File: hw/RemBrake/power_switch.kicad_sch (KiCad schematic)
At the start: 36 parts, among them Q5 BC337, Q6 SiS415DNT, Q7 BC847, Q8 BC337, Q9 BC847, U10 BD48ExxG, U3 TPS62140, U4 XC6220B331MR, U8 MAX40200AUK

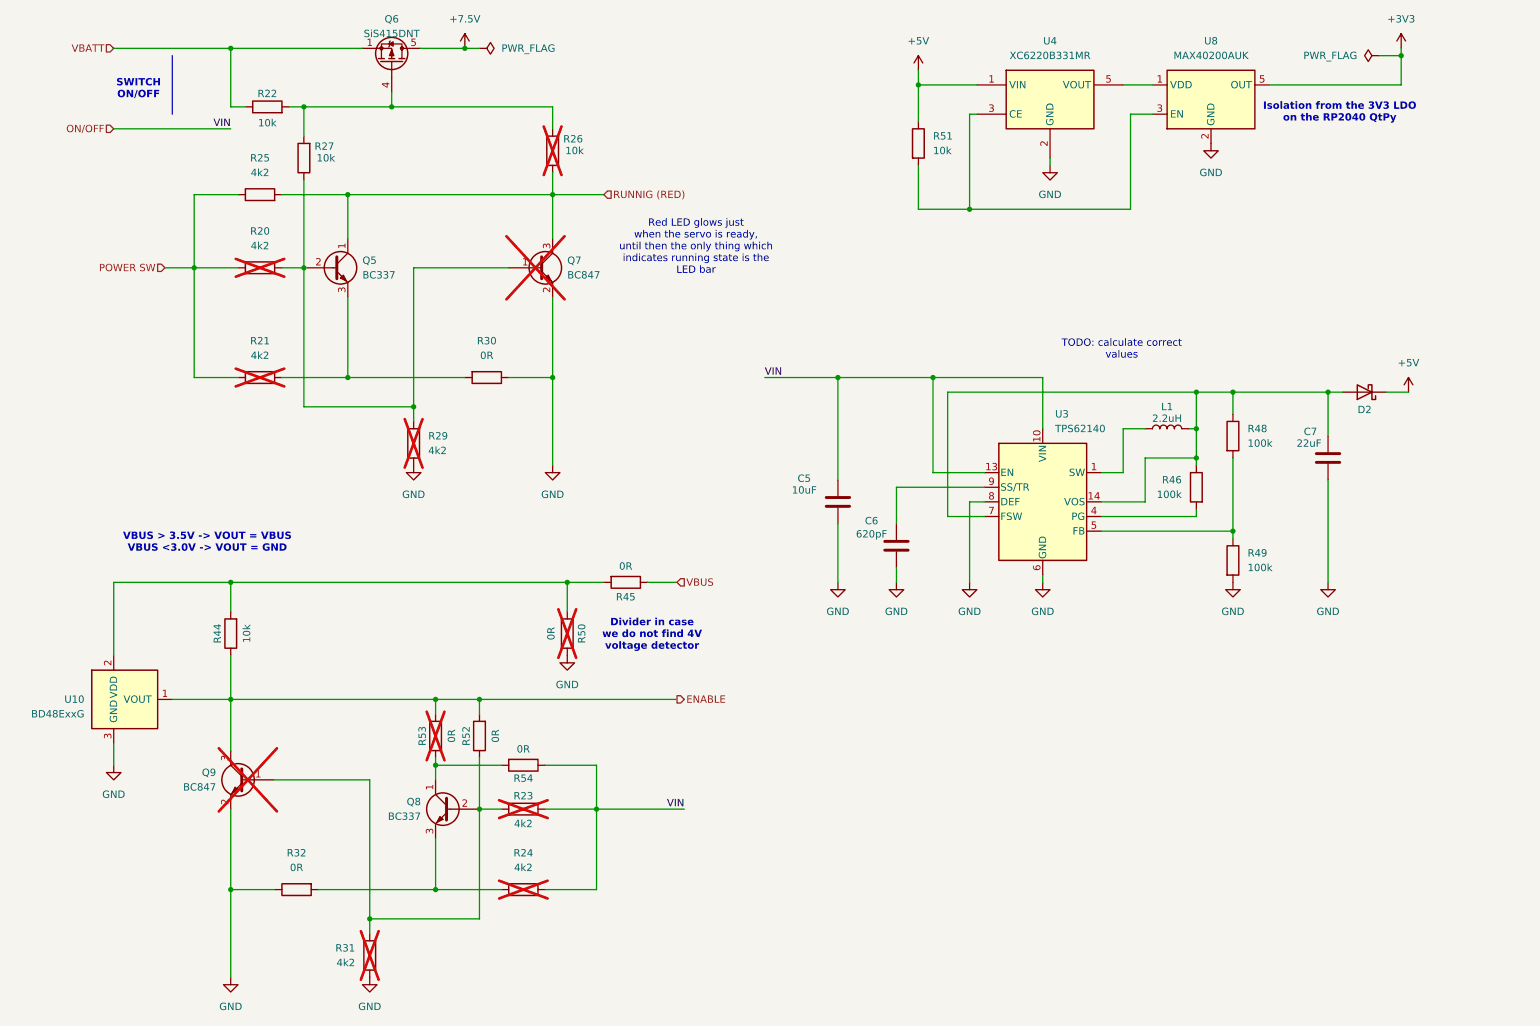
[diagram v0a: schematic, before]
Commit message: project renamed, schematics changed based on breakout boards notes and created new layout with better connectors
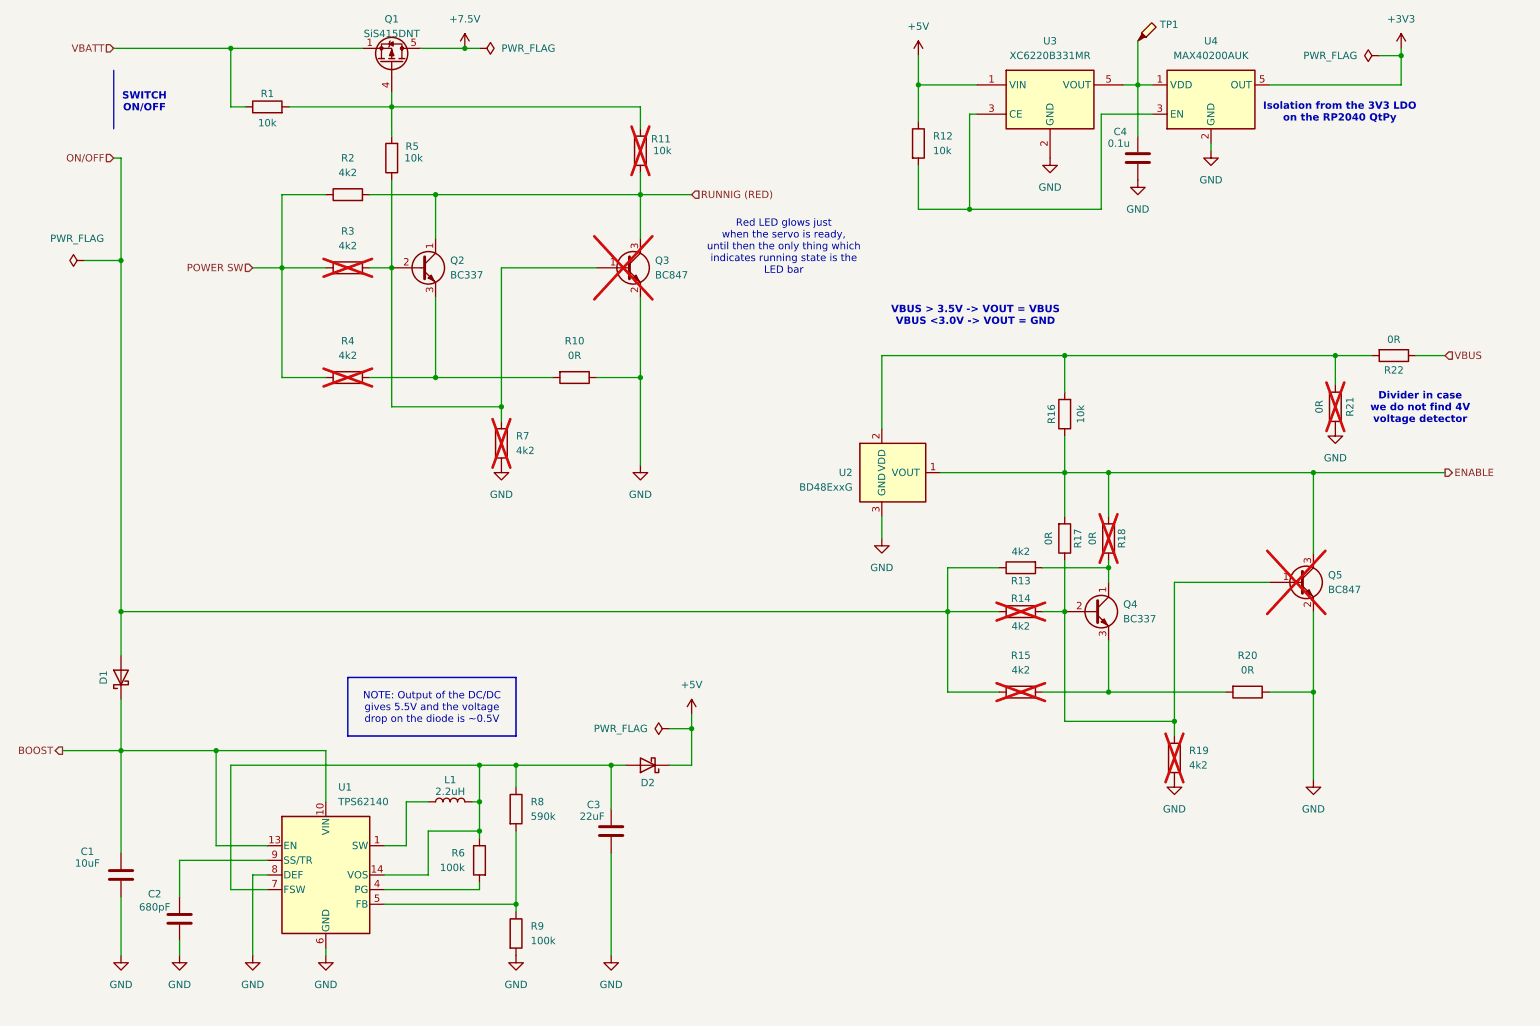
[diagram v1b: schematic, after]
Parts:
- added C4: 0.1u, Capacitor_SMD:C_0805_2012Metric_Pad1.18x1.45mm_HandSolder, symbol Device:C
- added D1: D_Schottky, Diode_SMD:D_SOD-128, symbol Device:D_Schottky
- added TP1: TestPoint_Probe, TestPoint:TestPoint_Pad_1.5x1.5mm, symbol Connector:TestPoint_Probe
- C2: renamed from C6; value 620pF -> 680pF
- D2: footprint (none) -> Diode_SMD:D_SOD-128; Purchase (none) -> https://cz.farnell.com/diodes-inc/mbr230s1f-7/schottky-rect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
- L1: footprint (none) -> Inductor_SMD:L_1008_2520Metric_Pad1.43x2.20mm_HandSolder; Purchase (none) -> https://cz.farnell.com/murata/dfe252012p-2r2m-p2/inductor-2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
- R13: renamed from R54; value 0R -> 4k2
- R8: renamed from R48; value 100k -> 590k
- renumbered C5 to C1, C7 to C3, Q6 to Q1, Q5 to Q2, Q7 to Q3, Q8 to Q4, Q9 to Q5, R22 to R1, R30 to R10, R26 to R11, R51 to R12, R23 to R14, R24 to R15, R44 to R16, R52 to R17, R53 to R18, R31 to R19, R25 to R2, R32 to R20, R50 to R21, R45 to R22, R20 to R3, R21 to R4, R27 to R5, R46 to R6, R29 to R7, R49 to R9, U3 to U1, U10 to U2, U4 to U3, U8 to U4
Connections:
- net GND: now also C4.2
- net ON/OFF: now also D1.2 (A); no longer C1.1, U1.10 (VIN), U1.11 (VIN), U1.12 (VIN), U1.13 (EN)
- net at U3.5 (VOUT), U4.1 (VDD): now also C4.1, TP1.1
- new net BOOST: C1.1, D1.1 (K), U1.10 (VIN), U1.11 (VIN), U1.12 (VIN), U1.13 (EN)
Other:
- note removed: "TODO: calculate correct values"
- moved on the sheet: C1, C2, C3, D2, L1, Q2, Q3, Q4, Q5, R10, R11, R13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

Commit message: added few components to fix indicator LED undefined cathode voltage and added vbus divider to match MCU voltage level
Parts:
- added R22: 10k, Resistor_SMD:R_0805_2012Metric_Pad1.20x1.40mm_HandSolder, symbol Device:R
- R7: value 4k2 -> 42k; now fitted
- renumbered R22 to R23
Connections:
- net ENABLE: now also R22.2
- net GND: now also R22.1
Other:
- note added: "Divide the VBUS to avoid busting the MCU"
- note added: "Divider for lower threshold voltage detectors"
- note added: "Red LED glows just when the servo is ready,until then the only thing whichindicates running state is the LED bar"
- note added: "TODO: add resistor to divide the vbus voltage"
- note removed: "Divider in case we do not find 4V voltage detector"
- note removed: "Red LED glows just when the servo is ready, until then the only thing which indicates running state is the LED bar"

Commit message: updated date and revision in the schematics
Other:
- company: (none) -> Pacner Bros Tech
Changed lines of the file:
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@@
 	(title_block
 		(title "Power Control")
-		(date "2024-12-15")
-		(rev "1.0")
+		(date "2025-02-23")
+		(rev "2.0")
+		(company "Pacner Bros Tech")
 	)
 	(text "VBUS > 3.5V -> VOUT = VBUS\nVBUS <3.0V -> VOUT = GND"

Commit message: updated annotation
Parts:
- added R11, R12: 0R, Resistor_SMD:R_0805_2012Metric_Pad1.20x1.40mm_HandSolder, symbol Device:R
- added R16, R2: 100k, Resistor_SMD:R_0805_2012Metric_Pad1.20x1.40mm_HandSolder, symbol Device:R
- C4: value 0.1u -> 0.1uF
- D1, D2: value D_Schottky -> MBR0520; footprint Diode_SMD:D_SOD-128 -> Diode_SMD:D_SOD-123
- Q3, Q5: now left out of the parts list
- R14: renamed from R11; now left out of the parts list
- R17: renamed from R13; value 4k2 -> 5k
- R18: renamed from R14; value 4k2 -> 5k; now left out of the parts list
- R19: renamed from R15; value 4k2 -> 5k; now left out of the parts list
- R22: renamed from R18; now left out of the parts list
- R23: renamed from R19; value 4k2 -> 5k; now left out of the parts list
- R25: renamed from R21; now left out of the parts list
- R3: renamed from R2; value 4k2 -> 5k
- R4: renamed from R3; value 4k2 -> 5k; now left out of the parts list
- R5: renamed from R4; value 4k2 -> 5k; now left out of the parts list
- R8: renamed from R7; value 42k -> 0R; now not fitted; now left out of the parts list
- renumbered R9 to R10, R10 to R13, R12 to R15, R16 to R20, R17 to R21, R20 to R24, R22 to R26, R23 to R27, R5 to R6, R6 to R7, R8 to R9
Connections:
- net GND: now also R16.1, R2.1
- net ON/OFF: now also R16.2
- net POWER SW: now also R2.2
- net RUNNIG (RED): now also R11.1, R12.1; no longer Q2.1 (C), R3.2
- net at Q2.2 (B), Q3.1 (B), R4.2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: now also R12.2
- new net: Q2.1 (C), R11.2, R3.2
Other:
- note removed: "TODO: add resistor to divide the vbus voltage"

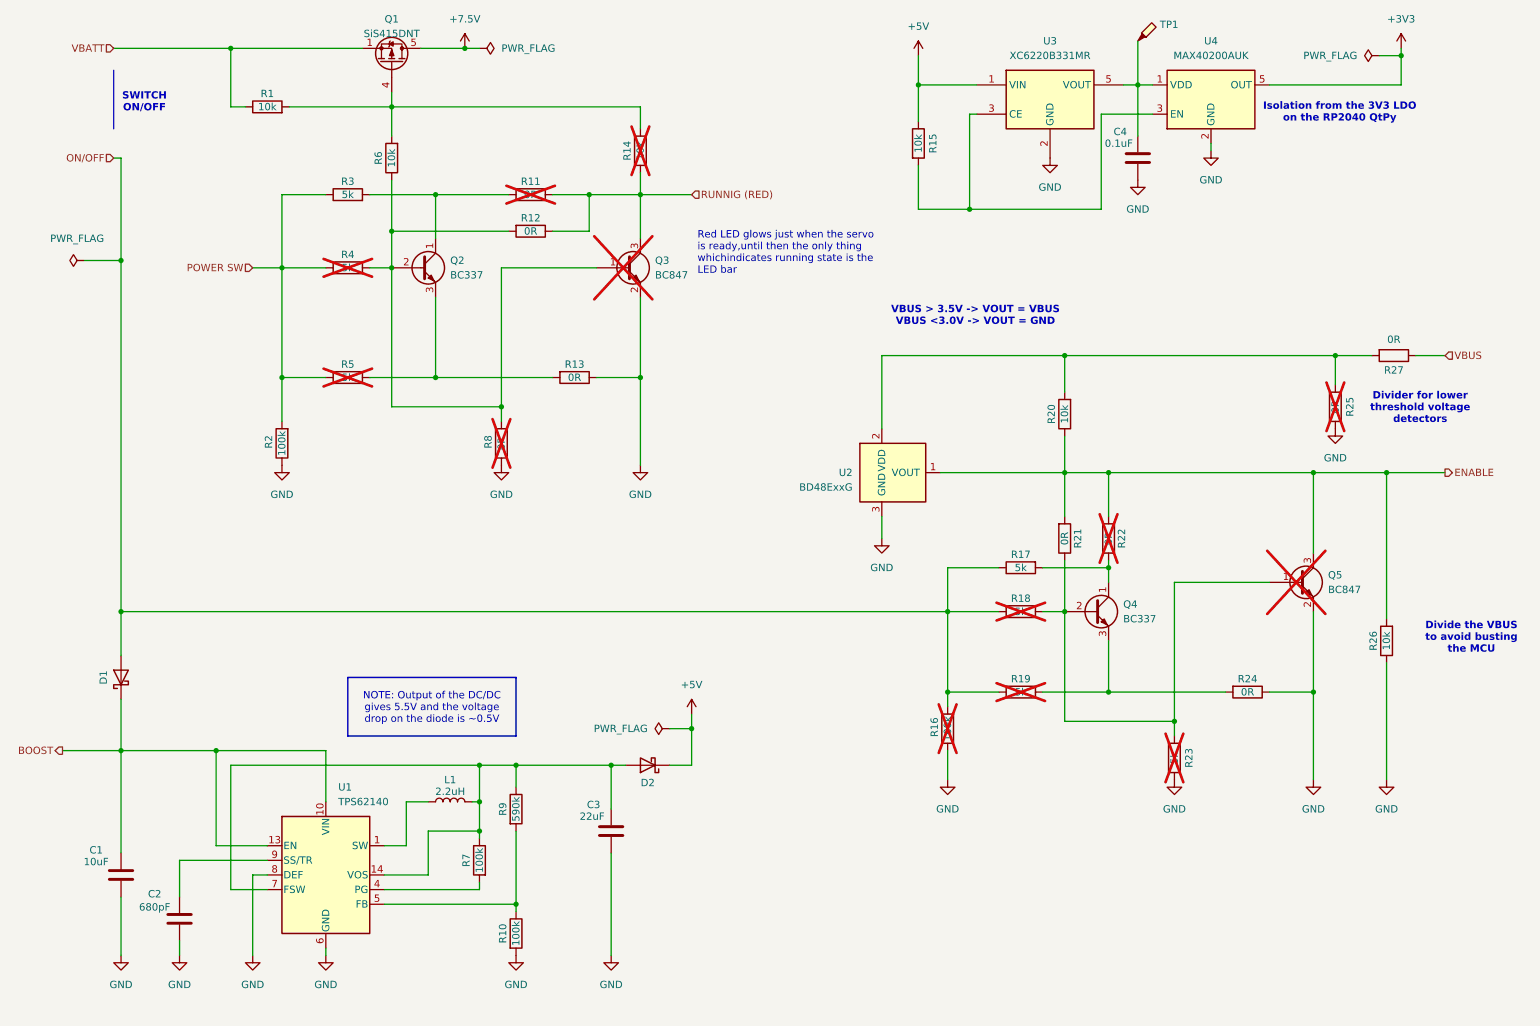
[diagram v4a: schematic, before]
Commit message: fixed bugs with LED reverse current leakage and beeper deterministic startup delay
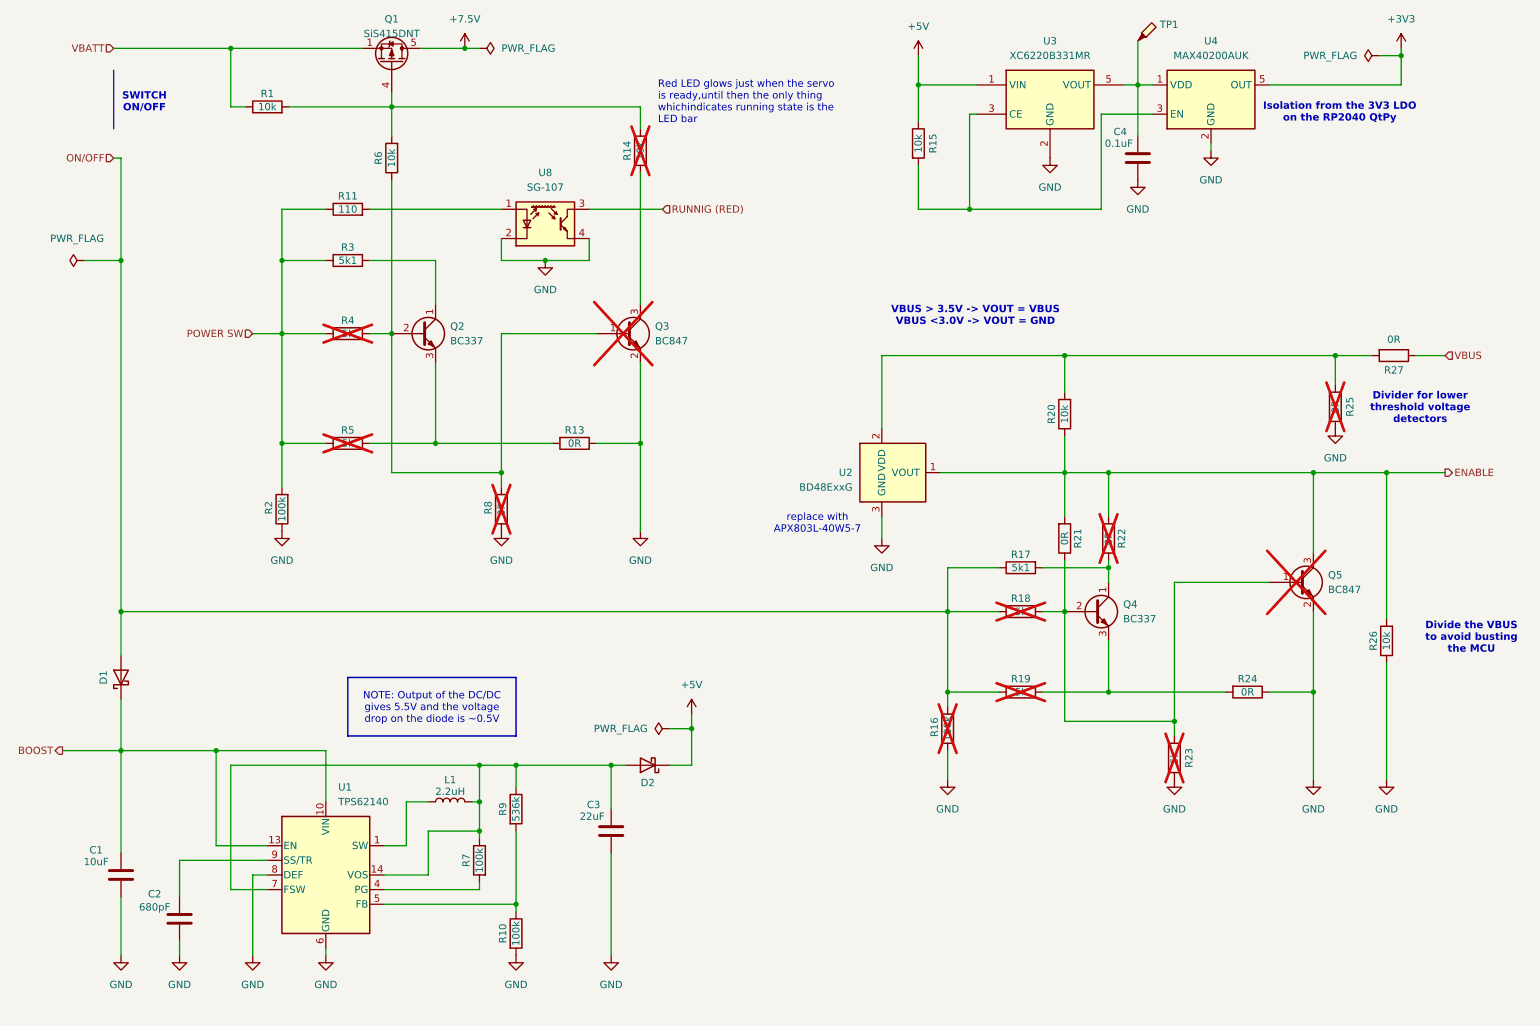
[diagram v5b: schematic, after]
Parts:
- removed R12: 0R, Resistor_SMD:R_0805_2012Metric_Pad1.20x1.40mm_HandSolder, symbol Device:R
- added U8: SG-107, OptoDevice:Kodenshi_SG105, symbol Sensor_Proximity:SG-107
- R11: value 0R -> 110; now fitted; now in the parts list
- R17, R3: value 5k -> 5k1
- R9: value 590k -> 536k
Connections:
- net GND: now also U8.2 (K), U8.4 (E)
- net POWER SW: now also R11.1
- net RUNNIG (RED): now also U8.3 (C); no longer Q3.3 (C), R11.1, R14.1
- net at Q2.1 (C), R3.2: no longer R11.2
- new net: Q3.3 (C), R14.1
- new net: R11.2, U8.1 (A)
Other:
- note added: "replace with APX803L-40W5-7"
- moved on the sheet: Q2, Q3, R13, R2, R3, R4, R5, R8

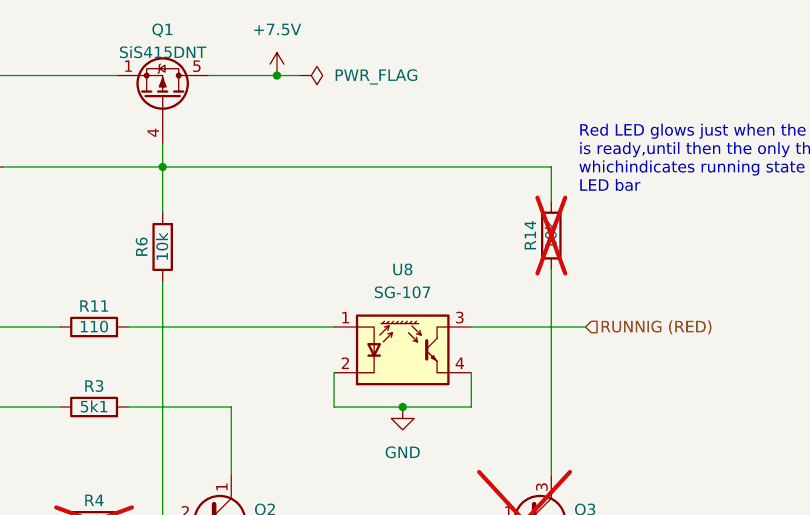
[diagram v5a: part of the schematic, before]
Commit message: updated pcb and added todo in the schematic
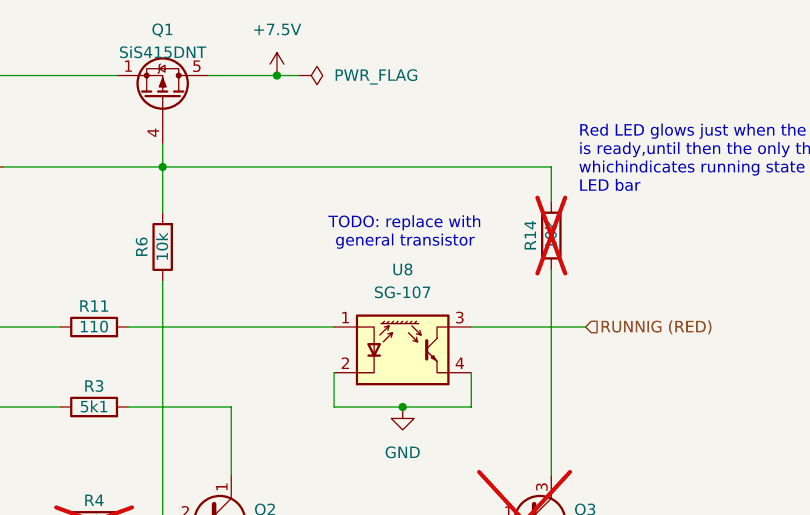
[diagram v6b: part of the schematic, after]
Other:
- note added: "TODO: replace with general transistor"
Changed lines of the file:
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@@
+		)
+	)
+	(text "TODO: replace with\ngeneral transistor"
+		(exclude_from_sim no)
+		(at 112.014 44.196 0)
+		(effects
+			(font
+				(size 1.27 1.27)
+			)
 		)
 	)
